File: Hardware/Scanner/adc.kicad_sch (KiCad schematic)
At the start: 9 parts, among them U2 NAU7802SGI, X1 4.9152 MHz

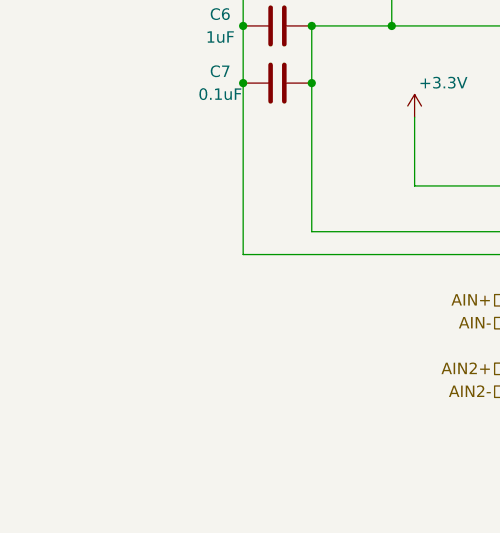
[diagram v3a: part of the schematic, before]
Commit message: updated schematic, and layout, updated bom, fully converted to 3.3v for Voltage input only
Signed-off-by: lokimetasmith <lokimail@gmail.com>
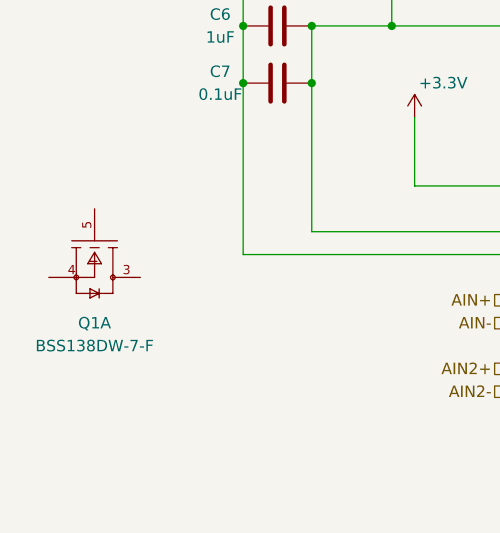
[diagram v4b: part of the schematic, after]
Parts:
- added Q1: BSS138DW-7-F, BSS138DW-7-F-A:Diodes_Inc._-_BSS138DW-7-F-A, symbol Diodes_Inc._-_BSS138DW-7-F:BSS138DW-7-F
- C10, C13, C7: digikey description (none) -> CAP CER 0.1UF 16V X7R 0603; digikey part number (none) -> 311-1088-1-ND
- C6: digikey description (none) -> CAP CER 1UF 16V X7R 0603; digikey part number (none) -> 311-1446-1-ND
- R18: digikey description (none) -> RES 1K OHM 1% 1/10W 0603; digikey part number (none) -> 311-1.00KHRCT-ND
- R6: digikey description (none) -> 0 Ohms Jumper 0.25W, 1/4W Chip Resistor 1206 (3216 Metric) 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; digikey part number (none) -> 4988-NRC12ZOTRFCT-ND; mouser description (none) -> CHP0603QFW-1R00ELF; mouser part number (none) -> 652-CHP0603QFW-1R00E
- X1: digikey description (none) -> XTAL OSC XO 4.9152MHZ CMOS SMD; digikey part number (none) -> 50-ECS-2520MVLC-049-BN-CT-ND
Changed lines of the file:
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@@
+      (effects (font (size 1.27 1.27)) hide)
+    )
+    (property "digikey description" "CAP CER 1UF 16V X7R 0603" (at 111.76 82.55 0)
+      (effects (font (size 1.27 1.27)) hide)
+    )
+    (property "digikey part number" "311-1446-1-ND" (at 111.76 82.55 0)
       (effects (font (size 1.27 1.27)) hide)
     )
@@
     )
     (property "Datasheet" "~" (at 177.8 93.98 0)
+      (effects (font (size 1.27 1.27)) hide)
+    )
+    (property "digikey description" "CAP CER 0.1UF 16V X7R 0603" (at 177.8 93.98 0)
+      (effects (font (size 1.27 1.27)) hide)
+    )
+    (property "digikey part number" "311-1088-1-ND" (at 177.8 93.98 0)
       (effects (font (size 1.27 1.27)) hide)
     )
@@
       (effects (font (size 1.27 1.27)) hide)
     )
+    (property "digikey description" "RES 1K OHM 1% 1/10W 0603" (at 233.68 107.95 0)
+      (effects (font (size 1.27 1.27)) hide)
+    )
+    (property "digikey part number" "311-1.00KHRCT-ND" (at 233.68 107.95 0)
+      (effects (font (size 1.27 1.27)) hide)
+    )
     (pin "1")
     (pin "2")
@@
     )
     (property "Datasheet" "~" (at 111.76 88.9 0)
+      (effects (font (size 1.27 1.27)) hide)
+    )
+    (property "digikey description" "CAP CER 0.1UF 16V X7R 0603" (at 111.76 88.9 0)
+      (effects (font (size 1.27 1.27)) hide)
+    )
+    (property "digikey part number" "311-1088-1-ND" (at 111.76 88.9 0)
       (effects (font (size 1.27 1.27)) hide)
     )
@@
       (effects (font (size 1.27 1.27)) hide)
     )
+    (property "digikey description" "XTAL OSC XO 4.9152MHZ CMOS SMD" (at 220.98 113.03 0)
+      (effects (font (size 1.27 1.27)) hide)
+    )
+    (property "digikey part number" "50-ECS-2520MVLC-049-BN-CT-ND" (at 220.98 113.03 0)
+      (effects (font (size 1.27 1.27)) hide)
+    )
     (pin "1")
     (pin "2")
@@
     )
   )
+  (symbol (lib_id "Diodes_Inc._-_BSS138DW-7-F:BSS138DW-7-F") (at 91.44 100.33 270) (unit 1)
+    (in_bom yes) (on_board yes) (dnp no) (fields_autoplaced)
+    (property "Reference" "Q1" (at 91.44 115.57 90)
+      (effects (font (size 1.27 1.27)))
+    )
+    (property "Value" "BSS138DW-7-F" (at 91.44 118.11 90)
+      (effects (font (size 1.27 1.27)))
+    )
+    (property "Footprint" "BSS138DW-7-F-A:Diodes_Inc._-_BSS138DW-7-F-A" (at 104.14 100.33 0)
+      (effects (font (size 1.27 1.27)) (justify left) hide)
+    )
+    (property "Datasheet" "https://www.diodes.com/assets/Datasheets/ds30203.pdf" (at 106.68 100.33 0)
+      (effects (font (size 1.27 1.27)) (justify left) hide)
+    )
+    (property "automotive" "No" (at 109.22 100.33 0)
+      (effects (font (size 1.27 1.27)) (justify left) hide)
+    )
+    (property "category" "Trans" (at 111.76 100.33 0)
+      (effects (font (size 1.27 1.27)) (justify left) hide)
+    )
+    (property "continuous drain current" "200mA" (at 114.3 100.33 0)
+      (effects (font (size 1.27 1.27)) (justify left) hide)
+    )
+    (property "depletion mode" "False" (at 116.84 100.33 0)
+      (effects (font (size 1.27 1.27)) (justify left) hide)
+    )
+    (property "device class L1" "Discrete Semiconductors" (at 119.38 100.33 0)
+      (effects (font (size 1.27 1.27)) (justify left) hide)
+    )
+    (property "device class L2" "Transistors" (at 121.92 100.33 0)
+      (effects (font (size 1.27 1.27)) (justify left) hide)
+    )
+    (property "device class L3" "MOSFETs" (at 124.46 100.33 0)
+      (effects (font (size 1.27 1.27)) (justify left) hide)
+    )
+    (property "digikey description" "MOSFET 2N-CH 50V 0.2A SC70-6" (at 127 100.33 0)
+      (effects (font (size 1.27 1.27)) (justify left) hide)
+    )
+    (property "digikey part number" "BSS138DW-FDICT-ND" (at 129.54 100.33 0)
+      (effects (font (size 1.27 1.27)) (justify left) hide)
+    )
+    (property "drain to source breakdown voltage" "75V" (at 132.08 100.33 0)
+      (effects (font (size 1.27 1.27)) (justify left) hide)
+    )
+    (property "drain to source resistance" "1.4Ω" (at 134.62 100.33 0)
+      (effects (font (size 1.27 1.27)) (justify left) hide)
+    )
+    (property "drain to source voltage" "50V" (at 137.16 100.33 0)
+      (effects (font (size 1.27 1.27)) (justify left) hide)
+    )
+    (property "footprint url" "https://www.diodes.com/assets/Package-Files/SOT363.pdf" (at 139.7 100.33 0)
+      (effects (font (size 1.27 1.27)) (justify left) hide)
+    )
+    (property "gate to source voltage" "20V" (at 142.24 100.33 0)
+      (effects (font (size 1.27 1.27)) (justify left) hide)
+    )
+    (property "height" "1.1mm" (at 144.78 100.33 0)
+      (effects (font (size 1.27 1.27)) (justify left) hide)
+    )
+    (property "input capacitace at vds" "50pF @ 10V" (at 147.32 100.33 0)
+      (effects (font (size 1.27 1.27)) (justify left) hide)
+    )
+    (property "lead free" "Yes" (at 149.86 100.33 0)
+      (effects (font (size 1.27 1.27)) (justify left) hide)
+    )
+    (property "library id" "315a08f55ef6fa24" (at 152.4 100.33 0)
+      (effects (font (size 1.27 1.27)) (justify left) hide)
+    )
+    (property "manufacturer" "Diodes Inc." (at 154.94 100.33 0)
+      (effects (font (size 1.27 1.27)) (justify left) hide)
+    )
+    (property "max junction temp" "+150°C" (at 157.48 100.33 0)
+      (effects (font (size 1.27 1.27)) (justify left) hide)
+    )
+    (property "mouser description" "MOSFET 50V 200mW" (at 160.02 100.33 0)
+      (effects (font (size 1.27 1.27)) (justify left) hide)
+    )
+    (property "mouser part number" "621-BSS138DW-F" (at 162.56 100.33 0)
+      (effects (font (size 1.27 1.27)) (justify left) hide)
+    )
+    (property "number of N channels" "2" (at 165.1 100.33 0)
+      (effects (font (size 1.27 1.27)) (justify left) hide)
+    )
+    (property "number of channels" "2" (at 167.64 100.33 0)
+      (effects (font (size 1.27 1.27)) (justify left) hide)
+    )
+    (property "package" "SOT363" (at 170.18 100.33 0)
+      (effects (font (size 1.27 1.27)) (justify left) hide)
+    )
+    (property "power dissipation" "200mW" (at 172.72 100.33 0)
+      (effects (font (size 1.27 1.27)) (justify left) hide)
+    )
+    (property "rohs" "Yes" (at 175.26 100.33 0)
+      (effects (font (size 1.27 1.27)) (justify left) hide)
+    )
+    (property "rthja max" "625°C/W" (at 177.8 100.33 0)
+      (effects (font (size 1.27 1.27)) (justify left) hide)
+    )
+    (property "standoff height" "0mm" (at 180.34 100.33 0)
+      (effects (font (size 1.27 1.27)) (justify left) hide)
+    )
+    (property "temperature range high" "+150°C" (at 182.88 100.33 0)
+      (effects (font (size 1.27 1.27)) (justify left) hide)
+    )
+    (property "temperature range low" "-55°C" (at 185.42 100.33 0)
+      (effects (font (size 1.27 1.27)) (justify left) hide)
+    )
+    (property "threshold vgs max" "1.5V" (at 187.96 100.33 0)
+      (effects (font (size 1.27 1.27)) (justify left) hide)
+    )
+    (property "threshold vgs min" "0.5V" (at 190.5 100.33 0)
+      (effects (font (size 1.27 1.27)) (justify left) hide)
+    )
+    (property "turn off delay time" "20ns" (at 193.04 100.33 0)
+      (effects (font (size 1.27 1.27)) (justify left) hide)
+    )
+    (property "turn on delay time" "20ns" (at 195.58 100.33 0)
+      (effects (font (size 1.27 1.27)) (justify left) hide)
+    )
+    (pin "3")
+    (pin "4")
+    (pin "5")
+    (pin "1")
+    (pin "2")
+    (pin "6")
+    (instances
+      (project "RoundScanner"
+        (path "/a818e058-3544-4da8-96fb-1a428660711f/f3879066-a91b-415e-b241-18f9d05de4a2"
+          (reference "Q1") (unit 1)
+        )
+        (path "/a818e058-3544-4da8-96fb-1a428660711f/a8dcb7a4-48cf-403e-b881-d44234291c62"
+          (reference "Q1") (unit 1)
+        )
+      )
+    )
+  )
   (symbol (lib_id "power:+3.3V") (at 220.98 100.33 0) (unit 1)
     (in_bom yes) (on_board yes) (dnp no)
@@
     )
     (property "Datasheet" "~" (at 124.46 68.58 0)
+      (effects (font (size 1.27 1.27)) hide)
+    )
+    (property "mouser description" "CHP0603QFW-1R00ELF" (at 124.46 68.58 0)
+      (effects (font (size 1.27 1.27)) hide)
+    )
+    (property "mouser part number" "652-CHP0603QFW-1R00E" (at 124.46 68.58 0)
+      (effects (font (size 1.27 1.27)) hide)
+    )
+    (property "digikey description" "0 Ohms Jumper 0.25W, 1/4W Chip Resistor 1206 (3216 Metric) Automotive AEC-Q200 Thick Film" (at 124.46 68.58 0)
+      (effects (font (size 1.27 1.27)) hide)
+    )
+    (property "digikey part number" "4988-NRC12ZOTRFCT-ND" (at 124.46 68.58 0)
       (effects (font (size 1.27 1.27)) hide)
     )
@@
       (effects (font (size 1.27 1.27)) hide)
     )
+    (property "digikey description" "CAP CER 0.1UF 16V X7R 0603" (at 242.57 114.3 0)
+      (effects (font (size 1.27 1.27)) hide)
+    )
+    (property "digikey part number" "311-1088-1-ND" (at 242.57 114.3 0)
+      (effects (font (size 1.27 1.27)) hide)
+    )

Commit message: updated red power led to a common lower value, dimmer power led shouldn't be an issue
Signed-off-by: lokimetasmith <lokimail@gmail.com>
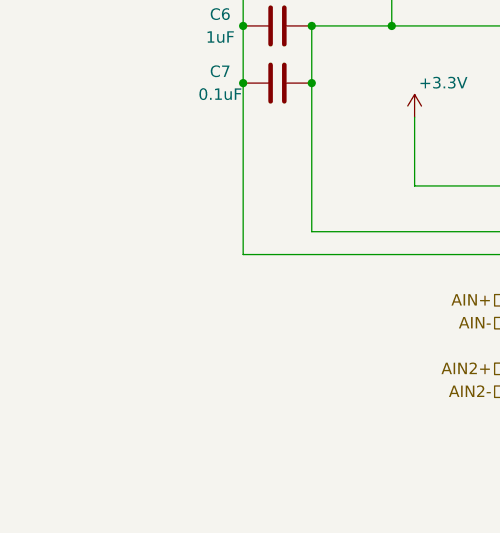
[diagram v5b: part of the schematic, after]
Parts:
- removed Q1: BSS138DW-7-F, BSS138DW-7-F-A:Diodes_Inc._-_BSS138DW-7-F-A, symbol Diodes_Inc._-_BSS138DW-7-F:BSS138DW-7-F
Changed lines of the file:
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@@
-    )
-  )
-  (symbol (lib_id "Diodes_Inc._-_BSS138DW-7-F:BSS138DW-7-F") (at 91.44 100.33 270) (unit 1)
-    (in_bom yes) (on_board yes) (dnp no) (fields_autoplaced)
-    (property "Reference" "Q1" (at 91.44 115.57 90)
-      (effects (font (size 1.27 1.27)))
-    )
-    (property "Value" "BSS138DW-7-F" (at 91.44 118.11 90)
-      (effects (font (size 1.27 1.27)))
-    )
-    (property "Footprint" "BSS138DW-7-F-A:Diodes_Inc._-_BSS138DW-7-F-A" (at 104.14 100.33 0)
-      (effects (font (size 1.27 1.27)) (justify left) hide)
-    )
-    (property "Datasheet" "https://www.diodes.com/assets/Datasheets/ds30203.pdf" (at 106.68 100.33 0)
-      (effects (font (size 1.27 1.27)) (justify left) hide)
-    )
-    (property "automotive" "No" (at 109.22 100.33 0)
-      (effects (font (size 1.27 1.27)) (justify left) hide)
-    )
-    (property "category" "Trans" (at 111.76 100.33 0)
-      (effects (font (size 1.27 1.27)) (justify left) hide)
-    )
-    (property "continuous drain current" "200mA" (at 114.3 100.33 0)
-      (effects (font (size 1.27 1.27)) (justify left) hide)
-    )
-    (property "depletion mode" "False" (at 116.84 100.33 0)
-      (effects (font (size 1.27 1.27)) (justify left) hide)
-    )
-    (property "device class L1" "Discrete Semiconductors" (at 119.38 100.33 0)
-      (effects (font (size 1.27 1.27)) (justify left) hide)
-    )
-    (property "device class L2" "Transistors" (at 121.92 100.33 0)
-      (effects (font (size 1.27 1.27)) (justify left) hide)
-    )
-    (property "device class L3" "MOSFETs" (at 124.46 100.33 0)
-      (effects (font (size 1.27 1.27)) (justify left) hide)
-    )
-    (property "digikey description" "MOSFET 2N-CH 50V 0.2A SC70-6" (at 127 100.33 0)
-      (effects (font (size 1.27 1.27)) (justify left) hide)
-    )
-    (property "digikey part number" "BSS138DW-FDICT-ND" (at 129.54 100.33 0)
-      (effects (font (size 1.27 1.27)) (justify left) hide)
-    )
-    (property "drain to source breakdown voltage" "75V" (at 132.08 100.33 0)
-      (effects (font (size 1.27 1.27)) (justify left) hide)
-    )
-    (property "drain to source resistance" "1.4Ω" (at 134.62 100.33 0)
-      (effects (font (size 1.27 1.27)) (justify left) hide)
-    )
-    (property "drain to source voltage" "50V" (at 137.16 100.33 0)
-      (effects (font (size 1.27 1.27)) (justify left) hide)
-    )
-    (property "footprint url" "https://www.diodes.com/assets/Package-Files/SOT363.pdf" (at 139.7 100.33 0)
-      (effects (font (size 1.27 1.27)) (justify left) hide)
-    )
-    (property "gate to source voltage" "20V" (at 142.24 100.33 0)
-      (effects (font (size 1.27 1.27)) (justify left) hide)
-    )
-    (property "height" "1.1mm" (at 144.78 100.33 0)
-      (effects (font (size 1.27 1.27)) (justify left) hide)
-    )
-    (property "input capacitace at vds" "50pF @ 10V" (at 147.32 100.33 0)
-      (effects (font (size 1.27 1.27)) (justify left) hide)
-    )
-    (property "lead free" "Yes" (at 149.86 100.33 0)
-      (effects (font (size 1.27 1.27)) (justify left) hide)
-    )
-    (property "library id" "315a08f55ef6fa24" (at 152.4 100.33 0)
-      (effects (font (size 1.27 1.27)) (justify left) hide)
-    )
-    (property "manufacturer" "Diodes Inc." (at 154.94 100.33 0)
-      (effects (font (size 1.27 1.27)) (justify left) hide)
-    )
-    (property "max junction temp" "+150°C" (at 157.48 100.33 0)
-      (effects (font (size 1.27 1.27)) (justify left) hide)
-    )
-    (property "mouser description" "MOSFET 50V 200mW" (at 160.02 100.33 0)
-      (effects (font (size 1.27 1.27)) (justify left) hide)
-    )
-    (property "mouser part number" "621-BSS138DW-F" (at 162.56 100.33 0)
-      (effects (font (size 1.27 1.27)) (justify left) hide)
-    )
-    (property "number of N channels" "2" (at 165.1 100.33 0)
-      (effects (font (size 1.27 1.27)) (justify left) hide)
-    )
-    (property "number of channels" "2" (at 167.64 100.33 0)
-      (effects (font (size 1.27 1.27)) (justify left) hide)
-    )
-    (property "package" "SOT363" (at 170.18 100.33 0)
-      (effects (font (size 1.27 1.27)) (justify left) hide)
-    )
-    (property "power dissipation" "200mW" (at 172.72 100.33 0)
-      (effects (font (size 1.27 1.27)) (justify left) hide)
-    )
-    (property "rohs" "Yes" (at 175.26 100.33 0)
-      (effects (font (size 1.27 1.27)) (justify left) hide)
-    )
-    (property "rthja max" "625°C/W" (at 177.8 100.33 0)
-      (effects (font (size 1.27 1.27)) (justify left) hide)
-    )
-    (property "standoff height" "0mm" (at 180.34 100.33 0)
-      (effects (font (size 1.27 1.27)) (justify left) hide)
-    )
-    (property "temperature range high" "+150°C" (at 182.88 100.33 0)
-      (effects (font (size 1.27 1.27)) (justify left) hide)
-    )
-    (property "temperature range low" "-55°C" (at 185.42 100.33 0)
-      (effects (font (size 1.27 1.27)) (justify left) hide)
-    )
-    (property "threshold vgs max" "1.5V" (at 187.96 100.33 0)
-      (effects (font (size 1.27 1.27)) (justify left) hide)
-    )
-    (property "threshold vgs min" "0.5V" (at 190.5 100.33 0)
-      (effects (font (size 1.27 1.27)) (justify left) hide)
-    )
-    (property "turn off delay time" "20ns" (at 193.04 100.33 0)
-      (effects (font (size 1.27 1.27)) (justify left) hide)
-    )
-    (property "turn on delay time" "20ns" (at 195.58 100.33 0)
-      (effects (font (size 1.27 1.27)) (justify left) hide)
-    )
-    (pin "3")
-    (pin "4")
-    (pin "5")
-    (pin "1")
-    (pin "2")
-    (pin "6")
-    (instances
-      (project "RoundScanner"
-        (path "/a818e058-3544-4da8-96fb-1a428660711f/f3879066-a91b-415e-b241-18f9d05de4a2"
-          (reference "Q1") (unit 1)
-        )
-        (path "/a818e058-3544-4da8-96fb-1a428660711f/a8dcb7a4-48cf-403e-b881-d44234291c62"
-          (reference "Q1") (unit 1)
-        )
-      )
     )
   )

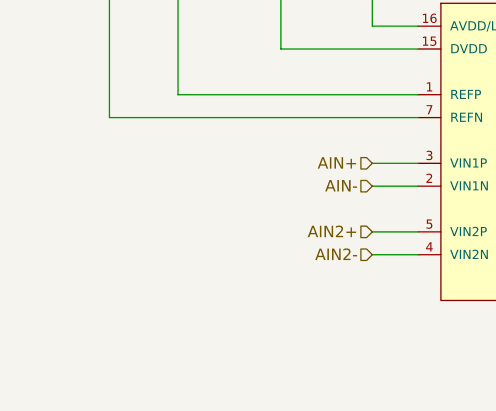
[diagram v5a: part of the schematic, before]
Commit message: added decoupling capactitors, added footprint for 3d model, need to verify new footprint
Signed-off-by: lokimetasmith <lokimail@gmail.com>
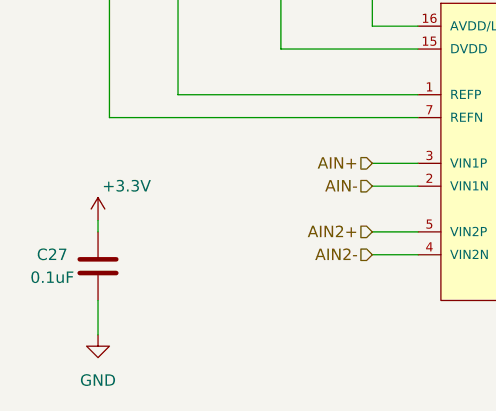
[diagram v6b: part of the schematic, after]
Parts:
- added C27: 0.1uF, Capacitor_SMD:C_0603_1608Metric_Pad1.08x0.95mm_HandSolder, symbol Device:C
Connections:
- net +3.3V: now also C27.2
- net GND: now also C27.1
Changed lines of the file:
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@@
+    (stroke (width 0) (type default))
+  )
+  (wire (pts (xy 106.68 128.27) (xy 106.68 132.08))
     (stroke (width 0) (type default))
   )
@@
   )
   (wire (pts (xy 242.57 100.33) (xy 242.57 110.49))
+    (stroke (width 0) (type default))
+  )
+  (wire (pts (xy 106.68 119.38) (xy 106.68 120.65))
     (stroke (width 0) (type default))
   )
@@
     )
   )
+  (symbol (lib_id "power:GND") (at 106.68 132.08 0) (unit 1)
+    (in_bom yes) (on_board yes) (dnp no) (fields_autoplaced)
+    (property "Reference" "#PWR040" (at 106.68 138.43 0)
+      (effects (font (size 1.27 1.27)) hide)
+    )
+    (property "Value" "GND" (at 106.68 137.16 0)
+      (effects (font (size 1.27 1.27)))
+    )
+    (property "Footprint" "" (at 106.68 132.08 0)
+      (effects (font (size 1.27 1.27)) hide)
+    )
+    (property "Datasheet" "" (at 106.68 132.08 0)
+      (effects (font (size 1.27 1.27)) hide)
+    )
+    (pin "1")
+    (instances
+      (project "RoundScanner"
+        (path "/a818e058-3544-4da8-96fb-1a428660711f/98df1e87-3735-4cb9-8253-663f6eb2234f"
+          (reference "#PWR040") (unit 1)
+        )
+        (path "/a818e058-3544-4da8-96fb-1a428660711f/a8dcb7a4-48cf-403e-b881-d44234291c62"
+          (reference "#PWR040") (unit 1)
+        )
+      )
+    )
+  )
+  (symbol (lib_id "Device:C") (at 106.68 124.46 180) (unit 1)
+    (in_bom yes) (on_board yes) (dnp no)
+    (property "Reference" "C27" (at 101.6 123.19 0)
+      (effects (font (size 1.27 1.27)))
+    )
+    (property "Value" "0.1uF" (at 101.6 125.73 0)
+      (effects (font (size 1.27 1.27)))
+    )
+    (property "Footprint" "Capacitor_SMD:C_0603_1608Metric_Pad1.08x0.95mm_HandSolder" (at 105.7148 120.65 0)
+      (effects (font (size 1.27 1.27)) hide)
+    )
+    (property "Datasheet" "~" (at 106.68 124.46 0)
+      (effects (font (size 1.27 1.27)) hide)
+    )
+    (property "digikey description" "CAP CER 0.1UF 16V X7R 0603" (at 106.68 124.46 0)
+      (effects (font (size 1.27 1.27)) hide)
+    )
+    (property "digikey part number" "311-1088-1-ND" (at 106.68 124.46 0)
+      (effects (font (size 1.27 1.27)) hide)
+    )
+    (pin "1")
+    (pin "2")
+    (instances
+      (project "RoundScanner"
+        (path "/a818e058-3544-4da8-96fb-1a428660711f/a8dcb7a4-48cf-403e-b881-d44234291c62"
+          (reference "C27") (unit 1)
+        )
+        (path "/a818e058-3544-4da8-96fb-1a428660711f/98df1e87-3735-4cb9-8253-663f6eb2234f"
+          (reference "C27") (unit 1)
+        )
+      )
+    )
+  )
   (symbol (lib_id "Device:R") (at 233.68 107.95 0) (mirror x) (unit 1)
     (in_bom yes) (on_board yes) (dnp no)
@@
         )
       )
+    )
+  )
+  (symbol (lib_id "power:+3.3V") (at 106.68 119.38 0) (unit 1)
+    (in_bom yes) (on_board yes) (dnp no)
+    (property "Reference" "#PWR032" (at 106.68 123.19 0)
+      (effects (font (size 1.27 1.27)) hide)
+    )
+    (property "Value" "+3.3V" (at 109.855 115.57 0)
+      (effects (font (size 1.27 1.27)))
+    )
+    (property "Footprint" "" (at 106.68 119.38 0)
+      (effects (font (size 1.27 1.27)) hide)
+    )
+    (property "Datasheet" "" (at 106.68 119.38 0)
+      (effects (font (size 1.27 1.27)) hide)
+    )
+    (pin "1")
+    (instances
+      (project "RoundScanner"
+        (path "/a818e058-3544-4da8-96fb-1a428660711f/98df1e87-3735-4cb9-8253-663f6eb2234f"
+          (reference "#PWR032") (unit 1)
+        )
+        (path "/a818e058-3544-4da8-96fb-1a428660711f/a8dcb7a4-48cf-403e-b881-d44234291c62"
+          (reference "#PWR032") (unit 1)
+        )
+      )
